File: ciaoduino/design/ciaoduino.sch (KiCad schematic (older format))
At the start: 22 parts, among them P1 ICSP, P2 CONN_01X02, P3 USB_OTG, P4 CONN_01X06, P5 CONN_01X06, P6 CONN_01X04, P7 CONN_01X14, Q1 Q_NMOS_DGS, SW1 SW_PUSH, SW2 SW_PUSH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

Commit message: Reorganize pinout.
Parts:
- added P8: CONN_01X07, Pin_Headers:Pin_Header_Straight_1x09, symbol CONN_01X09
- P7: value CONN_01X14 -> CONN_01X10; footprint Pin_Headers:Pin_Header_Straight_1x14 -> Pin_Headers:Pin_Header_Straight_1x12; symbol CONN_01X14 -> CONN_01X10
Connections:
- net ADC11: now also P7.10 (P10); no longer P7.11 (P11)
- net ADC8: now also P7.9 (P9); no longer P7.14 (P14)
- net GND: now also P8.2 (P2)
- net VCC: now also P8.1 (P1)
- net INT6: now reaches U2.1 ((INT6/AIN0)PE6)
- net INT6: now also P8.9 (P9)
- net PWN_3A: now reaches U2.31 ((OC3A/~OC4A~)PC6)
- net PWN_3A: now also P8.5 (P5)
- net PWN_4A: now reaches U2.32 ((ICP3/CLK0/OC4A)PC7)
- net PWN_4A: now also P8.6 (P6)
- net ADC10 renamed PWM_4D
- net PWM_4D: now also P8.8 (P8); no longer P7.12 (P12)
- net ADC12 renamed PWN_1A
- net PWN_1A: now also P8.3 (P3); no longer P7.10 (P10)
- net ADC13 renamed PWN_1B
- net PWN_1B: now also P8.4 (P4); no longer P7.9 (P9)
- net ADC9 renamed ~PWM_4D
- net ~PWM_4D: now also P8.7 (P7); no longer P7.13 (P13)
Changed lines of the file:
@@
 SCLK
 $Comp
-L CONN_01X14 P7
+L CONN_01X10 P7
 U 1 1 570D5BA0
-P 3550 1550
-F 0 "P7" H 3550 2300 50  0000 C CNN
-F 1 "CONN_01X14" V 3650 1550 50  0000 C CNN
-F 2 "Pin_Headers:Pin_Header_Straight_1x14" H 3550 1550 50  0001 C CNN
-F 3 "" H 3550 1550 50  0000 C CNN
-	1    3550 1550
+P 10400 2100
+F 0 "P7" H 10400 2850 50  0000 C CNN
+F 1 "CONN_01X10" V 10500 2100 50  0000 C CNN
+F 2 "Pin_Headers:Pin_Header_Straight_1x12" H 10400 2100 50  0001 C CNN
+F 3 "" H 10400 2100 50  0000 C CNN
+	1    10400 2100
 	1    0    0    -1
 $EndComp
@@
 L VCC #PWR018
 U 1 1 570D5FF9
-P 3200 700
-F 0 "#PWR018" H 3200 550 50  0001 C CNN
-F 1 "VCC" H 3200 850 50  0000 C CNN
-F 2 "" H 3200 700 50  0000 C CNN
-F 3 "" H 3200 700 50  0000 C CNN
-	1    3200 700
+P 10050 1450
+F 0 "#PWR018" H 10050 1300 50  0001 C CNN
+F 1 "VCC" H 10050 1600 50  0000 C CNN
+F 2 "" H 10050 1450 50  0000 C CNN
+F 3 "" H 10050 1450 50  0000 C CNN
+	1    10050 1450
 	1    0    0    -1
 $EndComp
@@
 L GND #PWR019
 U 1 1 570D5FFF
-P 2750 800
-F 0 "#PWR019" H 2750 550 50  0001 C CNN
-F 1 "GND" H 2750 650 50  0000 C CNN
-F 2 "" H 2750 800 50  0000 C CNN
-F 3 "" H 2750 800 50  0000 C CNN
-	1    2750 800
+P 9600 1550
+F 0 "#PWR019" H 9600 1300 50  0001 C CNN
+F 1 "GND" H 9600 1400 50  0000 C CNN
+F 2 "" H 9600 1550 50  0000 C CNN
+F 3 "" H 9600 1550 50  0000 C CNN
+	1    9600 1550
 	1    0    0    -1
 $EndComp
@@
 Text GLabel 5900 4550 2    60   Input ~ 0
 ADC8
-Text GLabel 5900 4750 2    60   Input ~ 0
-ADC9
-Text GLabel 5900 4850 2    60   Input ~ 0
-ADC10
 Text GLabel 5950 3350 2    60   Input ~ 0
 ADC11
-Text GLabel 5950 3450 2    60   Input ~ 0
-ADC12
-Text GLabel 5950 3550 2    60   Input ~ 0
-ADC13
-Text GLabel 3200 1100 0    60   Input ~ 0
+Text GLabel 10050 1850 0    60   Input ~ 0
 ADC0
-Text GLabel 3200 1200 0    60   Input ~ 0
+Text GLabel 10050 1950 0    60   Input ~ 0
 ADC1
-Text GLabel 3200 1300 0    60   Input ~ 0
+Text GLabel 10050 2050 0    60   Input ~ 0
 ADC4
-Text GLabel 3200 1400 0    60   Input ~ 0
+Text GLabel 10050 2150 0    60   Input ~ 0
 ADC5
-Text GLabel 3200 1500 0    60   Input ~ 0
+Text GLabel 10050 2250 0    60   Input ~ 0
 ADC6
-Text GLabel 3200 1600 0    60   Input ~ 0
+Text GLabel 10050 2350 0    60   Input ~ 0
 ADC7
-Text GLabel 3200 2200 0    60   Input ~ 0
+Text GLabel 10000 2450 0    60   Input ~ 0
 ADC8
-Text GLabel 3200 2100 0    60   Input ~ 0
-ADC9
-Text GLabel 3200 2000 0    60   Input ~ 0
-ADC10
-Text GLabel 3200 1900 0    60   Input ~ 0
+Text GLabel 10050 2550 0    60   Input ~ 0
 ADC11
-Text GLabel 3200 1800 0    60   Input ~ 0
-ADC12
-Text GLabel 3200 1700 0    60   Input ~ 0
-ADC13
 Wire Wire Line
 	6500 4500 6500 4650
@@
 	7950 1950 7850 1950
 Wire Wire Line
-	3200 700  3200 900
-Wire Wire Line
-	3200 900  3350 900
-Wire Wire Line
-	2750 800  3100 800
-Wire Wire Line
-	3100 800  3100 1000
-Wire Wire Line
-	3100 1000 3350 1000
+	10050 1450 10050 1650
+Wire Wire Line
+	10050 1650 10200 1650
+Wire Wire Line
+	9600 1550 9950 1550
+Wire Wire Line
+	9950 1550 9950 1750
 Wire Wire Line
 	5850 5350 5950 5350
@@
 	5950 3350 5850 3350
 Wire Wire Line
-	5950 3450 5850 3450
-Wire Wire Line
-	5950 3550 5850 3550
+	5850 3450 6000 3450
+Wire Wire Line
+	5850 3550 6000 3550
 Wire Wire Line
 	5900 4550 5850 4550
 Wire Wire Line
-	5900 4750 5850 4750
-Wire Wire Line
-	5900 4850 5850 4850
-Wire Wire Line
-	3200 1600 3350 1600
-Wire Wire Line
-	3200 1500 3350 1500
-Wire Wire Line
-	3200 1400 3350 1400
-Wire Wire Line
-	3200 1300 3350 1300
-Wire Wire Line
-	3200 1200 3350 1200
-Wire Wire Line
-	3200 1100 3350 1100
-Wire Wire Line
-	3200 1700 3350 1700
-Wire Wire Line
-	3200 1800 3350 1800
-Wire Wire Line
-	3200 1900 3350 1900
-Wire Wire Line
-	3200 2000 3350 2000
-Wire Wire Line
-	3200 2100 3350 2100
-Wire Wire Line
-	3200 2200 3350 2200
+	5850 4750 6000 4750
+Wire Wire Line
+	5850 4850 6000 4850
 Wire Wire Line
 	2350 4950 1550 4950
@@
 	1    0    0    -1
 $EndComp
+Text GLabel 6000 4850 2    39   Input ~ 0
+PWM_4D
+Text GLabel 6000 4750 2    39   Input ~ 0
+~PWM_4D
+Text GLabel 6000 3850 2    39   Input ~ 0
+PWN_3A
+Text GLabel 6000 3950 2    39   Input ~ 0
+PWN_4A
+Text GLabel 6000 3450 2    39   Input ~ 0
+PWN_1A
+Text GLabel 6000 3550 2    39   Input ~ 0
+PWN_1B
+Wire Wire Line
+	6000 3850 5850 3850
+Wire Wire Line
+	6000 3950 5850 3950
+$Comp
+L CONN_01X09 P8
+U 1 1 58656EA3
+P 10450 4000
+F 0 "P8" H 10450 4400 50  0000 C CNN
+F 1 "CONN_01X07" V 10550 4000 50  0000 C CNN
+F 2 "Pin_Headers:Pin_Header_Straight_1x09" H 10450 4000 50  0001 C CNN
+F 3 "" H 10450 4000 50  0000 C CNN
+	1    10450 4000
+	1    0    0    -1
+$EndComp
+$Comp
+L VCC #PWR024
+U 1 1 5865719B
+P 10000 3500
+F 0 "#PWR024" H 10000 3350 50  0001 C CNN
+F 1 "VCC" H 10000 3650 50  0000 C CNN
+F 2 "" H 10000 3500 50  0000 C CNN
+F 3 "" H 10000 3500 50  0000 C CNN
+	1    10000 3500
+	1    0    0    -1
+$EndComp
+$Comp
+L GND #PWR025
+U 1 1 586571EB
+P 9700 3550
+F 0 "#PWR025" H 9700 3300 50  0001 C CNN
+F 1 "GND" H 9700 3400 50  0000 C CNN
+F 2 "" H 9700 3550 50  0000 C CNN
+F 3 "" H 9700 3550 50  0000 C CNN
+	1    9700 3550
+	1    0    0    -1
+$EndComp
+Wire Wire Line
+	10000 3600 10000 3500
+Wire Wire Line
+	9700 3550 9950 3550
+Wire Wire Line
+	9950 3550 9950 3700
+Wire Wire Line
+	10000 3600 10250 3600
+Wire Wire Line
+	9950 3700 10250 3700
+Text GLabel 10050 3800 0    39   Input ~ 0
+PWN_1A
+Text GLabel 10050 3900 0    39   Input ~ 0
+PWN_1B
+Text GLabel 10050 4000 0    39   Input ~ 0
+PWN_3A
+Text GLabel 10050 4100 0    39   Input ~ 0
+PWN_4A
+Text GLabel 10050 4200 0    39   Input ~ 0
+~PWM_4D
+Text GLabel 10050 4300 0    39   Input ~ 0
+PWM_4D
+Text GLabel 6000 5150 2    39   Input ~ 0
+INT6
+Wire Wire Line
+	6000 5150 5850 5150
+Text GLabel 10050 4400 0    39   Input ~ 0
+INT6
+Wire Wire Line
+	10050 3800 10250 3800
+Wire Wire Line
+	10050 3900 10250 3900
+Wire Wire Line
+	10050 4000 10250 4000
+Wire Wire Line
+	10050 4100 10250 4100
+Wire Wire Line
+	10050 4200 10250 4200
+Wire Wire Line
+	10050 4300 10250 4300
+Wire Wire Line
+	10050 4400 10250 4400
+Wire Wire Line
+	9950 1750 10200 1750
+Wire Wire Line
+	10050 1850 10200 1850
+Wire Wire Line
+	10050 1950 10200 1950
+Wire Wire Line
+	10050 2050 10200 2050
+Wire Wire Line
+	10050 2150 10200 2150
+Wire Wire Line
+	10050 2250 10200 2250
+Wire Wire Line
+	10050 2350 10200 2350
+Wire Wire Line
+	10000 2450 10200 2450
+Wire Wire Line
+	10050 2550 10200 2550
 $EndSCHEMATC

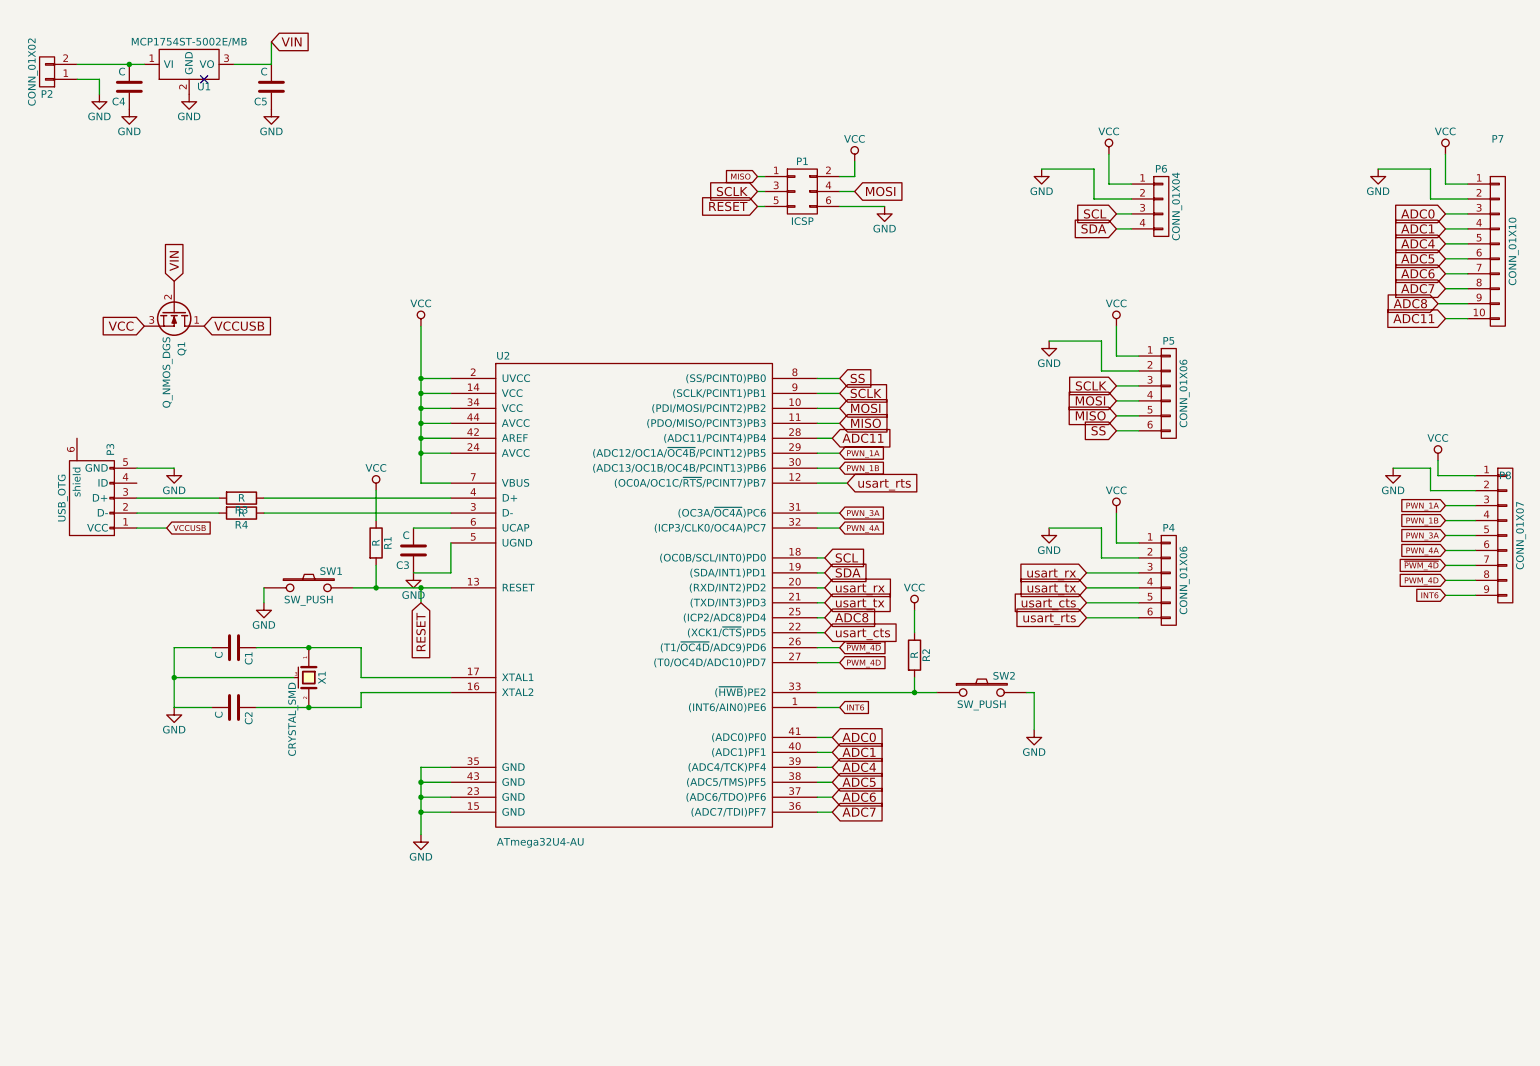
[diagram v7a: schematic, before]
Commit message: ciaoduino: complete a messy routing.
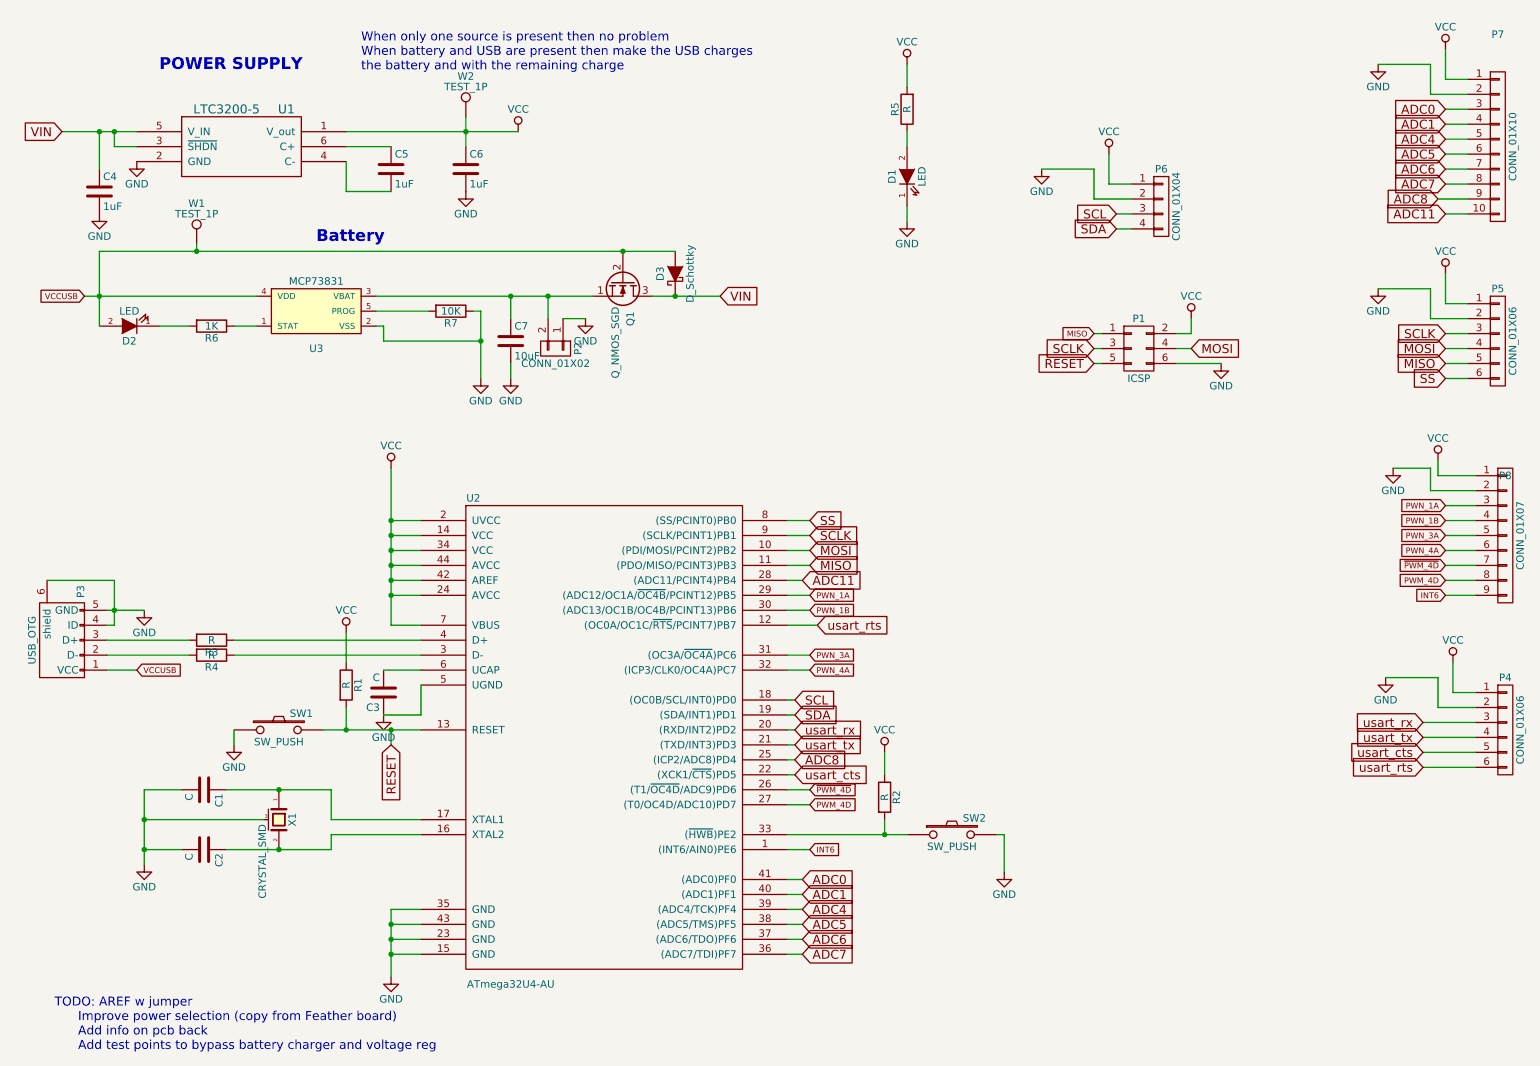
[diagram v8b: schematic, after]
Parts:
- removed Q1: Q_NMOS_DGS, TO_SOT_Packages_SMD:SOT-23, symbol Q_NMOS_DGS
- removed U1: MCP1754ST-5002E/MB, TO_SOT_Packages_SMD:SOT-323, symbol MCP1754ST-5002E/MB
- added C6: 1uF, Capacitors_SMD:C_0603_HandSoldering, symbol C
- added C7: 10uF, Capacitors_SMD:C_0603_HandSoldering, symbol C
- added D1, D2: LED, LEDs:LED_0603, symbol LED
- added D3: D_Schottky, Diodes_SMD:DO-214AB, symbol D_Schottky
- added Q1: Q_NMOS_SGD, TO_SOT_Packages_SMD:SOT-23, symbol Q_NMOS_SGD
- added R5: R, Resistors_SMD:R_0603, symbol R
- added R6: 1K, Resistors_SMD:R_0603_HandSoldering, symbol R
- added R7: 10K, Resistors_SMD:R_0603_HandSoldering, symbol R
- added U1: LTC3200-5, TO_SOT_Packages_SMD:SOT-23-6_Handsoldering, symbol LTC3200-5
- added U3: MCP73831, TO_SOT_Packages_SMD:SOT-23-5, symbol MCP73831
- added W1, W2: TEST_1P, SMD_Packages:1Pin, symbol TEST_1P
- C4, C5: value C -> 1uF
- P1: footprint Pin_Headers:Pin_Header_Straight_2x03 -> ciaoduino:ICSP_SMD
- P7: footprint Pin_Headers:Pin_Header_Straight_1x12 -> Pin_Headers:Pin_Header_Straight_1x10
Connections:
- net GND: now also C4.2, P3.4 (ID), P3.6 (shield), C6.2, C7.2, D1.1 (K), R7.1, U1.2 (GND), U3.2 (VSS); no longer C4.1, C5.1
- net VCC: now also C6.1, R5.2, U1.1 (V_out), W2.1
- net VCCUSB: now also D2.2 (A), D3.2 (A), Q1.2 (G), U3.4 (VDD), W1.1
- net VIN: now also C4.1, D3.1 (K), Q1.3 (D), U1.3 (~SHDN), U1.5 (V_IN); no longer C5.2
- net at P2.2 (P2): now also C7.1, Q1.1 (S), U3.3 (VBAT); no longer C4.2
- new net: D1.2 (A), R5.1
- new net: R6.1, U3.1 (STAT)
- new net: R7.2, U3.5 (PROG)
- new net: C5.2, U1.4 (C-)
- new net: C5.1, U1.6 (C+)
- new net: D2.1 (K), R6.2
- no-connect marks 1 -> 0
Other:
- note added: "Battery\n"
- note added: "POWER SUPPLY"
- note added: "TODO: AREF w jumper\n Improve power selection (copy from Feather board)\n Add info on pcb back\n Add test points to bypass battery charger and voltage reg\n"
- note added: "When only one source is present then no problem\nWhen battery and USB are present then make the USB charges\nthe battery and with the remaining charge"
- moved on the sheet: C1, C2, C3, P1, P2, P3, P4, P5, P7, R1, R2, R3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
